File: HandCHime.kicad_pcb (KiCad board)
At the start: 4 copper layers, 38.1 x 22.6 mm, 18 parts, among them J1 USB_C_Receptacle_USB2.0, J2 Pins, SW0 BOOT, SW1 Row 0, Col 0, SW2 Row 0, Col 1, U1 CH552T, U2 USBLC6-2P6

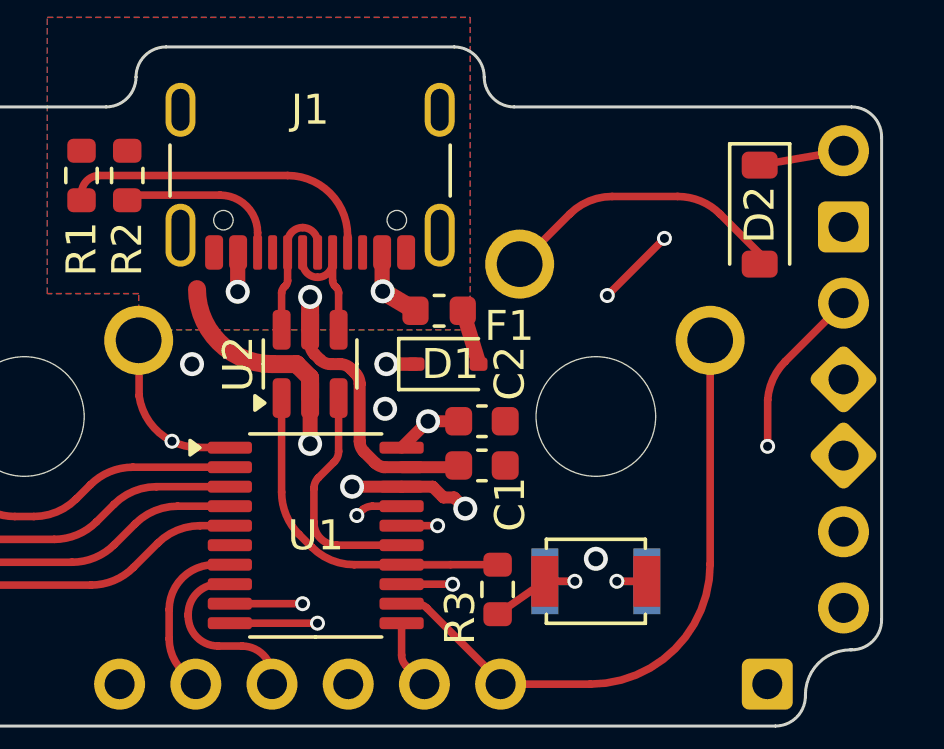
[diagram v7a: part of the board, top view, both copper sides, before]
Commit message: Use smaller ESD chip
USBLC6-2SC6 → PRTR5V0U2X
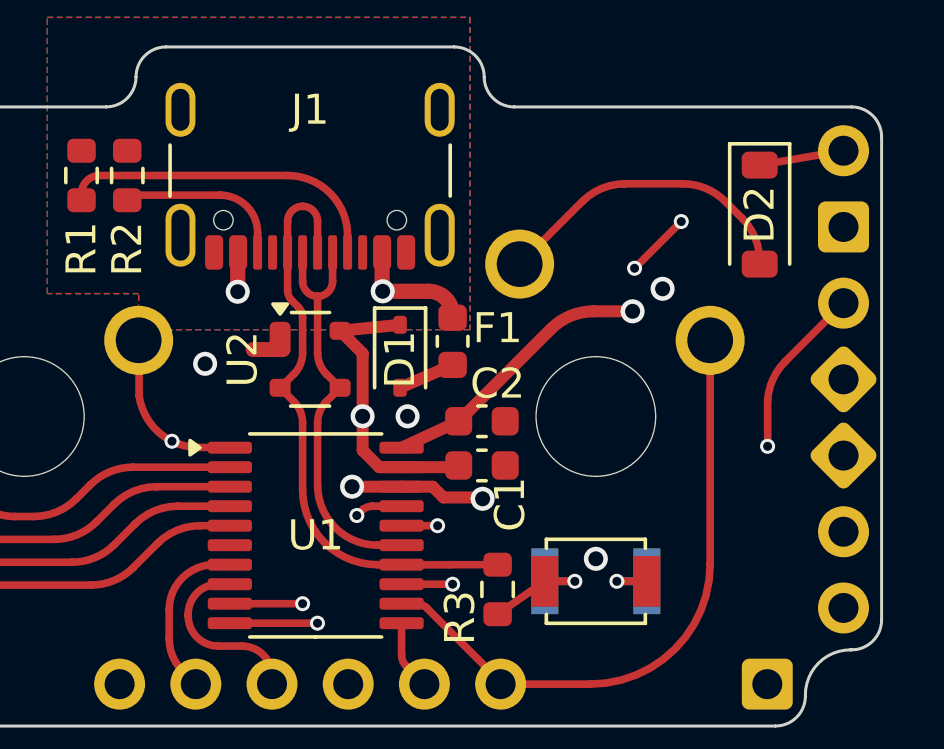
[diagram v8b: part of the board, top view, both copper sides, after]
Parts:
- U2: value USBLC6-2P6 -> PRTR5V0U2X; footprint Package_TO_SOT_SMD:SOT-23-6 -> Package_TO_SOT_SMD:SOT-143
- moved NT1 2.99 mm to (157.4, 47.8), turned to 180 degrees
- moved D1 1.58 mm to (161.8, 48.0), turned to -90 degrees
- moved F1 1.11 mm to (163.5, 47.5), turned to -90 degrees
- moved U2 0.15 mm to (158.8, 48.1), turned to 0 degrees
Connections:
- J1 pad A6: USB_C+ -> USB+
- J1 pad A7: USB_C- -> USB-
- J1 pad B6: USB_C+ -> USB+
- J1 pad B7: USB_C- -> USB-
- U2 pad 1: USB+ -> GNDPWR
- U2 pad 2: GNDPWR -> USB+
- U2 pad 4: USB_C- -> VCC
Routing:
- net USB+: track 8.43 -> 16.9 mm
- net USB-: track 7.76 -> 14.2 mm
- net GNDPWR: track 5.96 -> 0.00 mm
- net USB_C-: track 4.17 -> 0.00 mm
- net USB_C+: track 4.17 -> 0.00 mm
- net VCC: track 53.8 -> 51.5 mm, vias 2 -> 1
- net VBUS: track 9.33 -> 11.0 mm
- net GND: track 6.08 -> 4.52 mm
- net Net-(D2-A): track 9.88 -> 10.5 mm
- net R0: track 59.6 -> 59.0 mm
